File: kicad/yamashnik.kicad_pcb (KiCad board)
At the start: 2 copper layers, 43 x 25.8 mm, 13 parts, among them J1 USB_AM_PCB, P1 CONN_5, P2 CONN_4, U1 6N137, U2 6N138, U3 CP2102

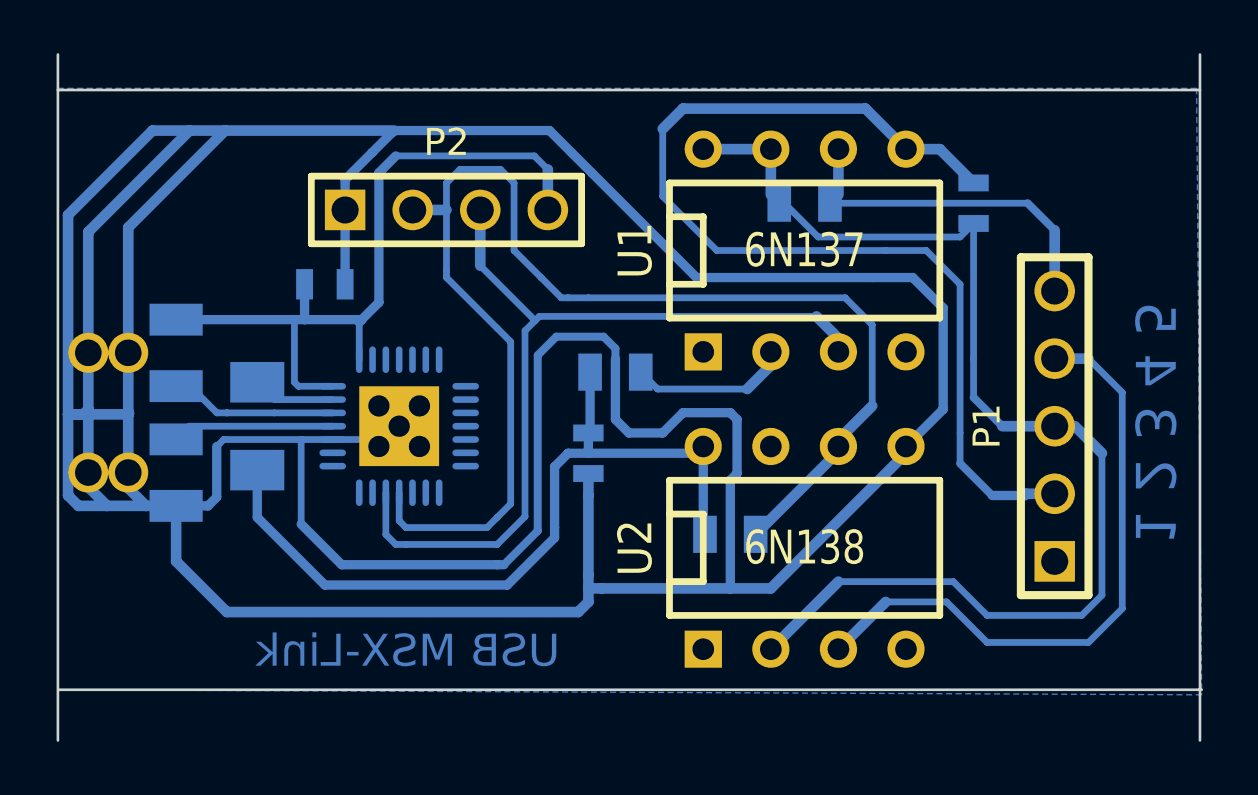
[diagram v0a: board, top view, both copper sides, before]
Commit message: recovered kicad_pcb, updated edge cuts
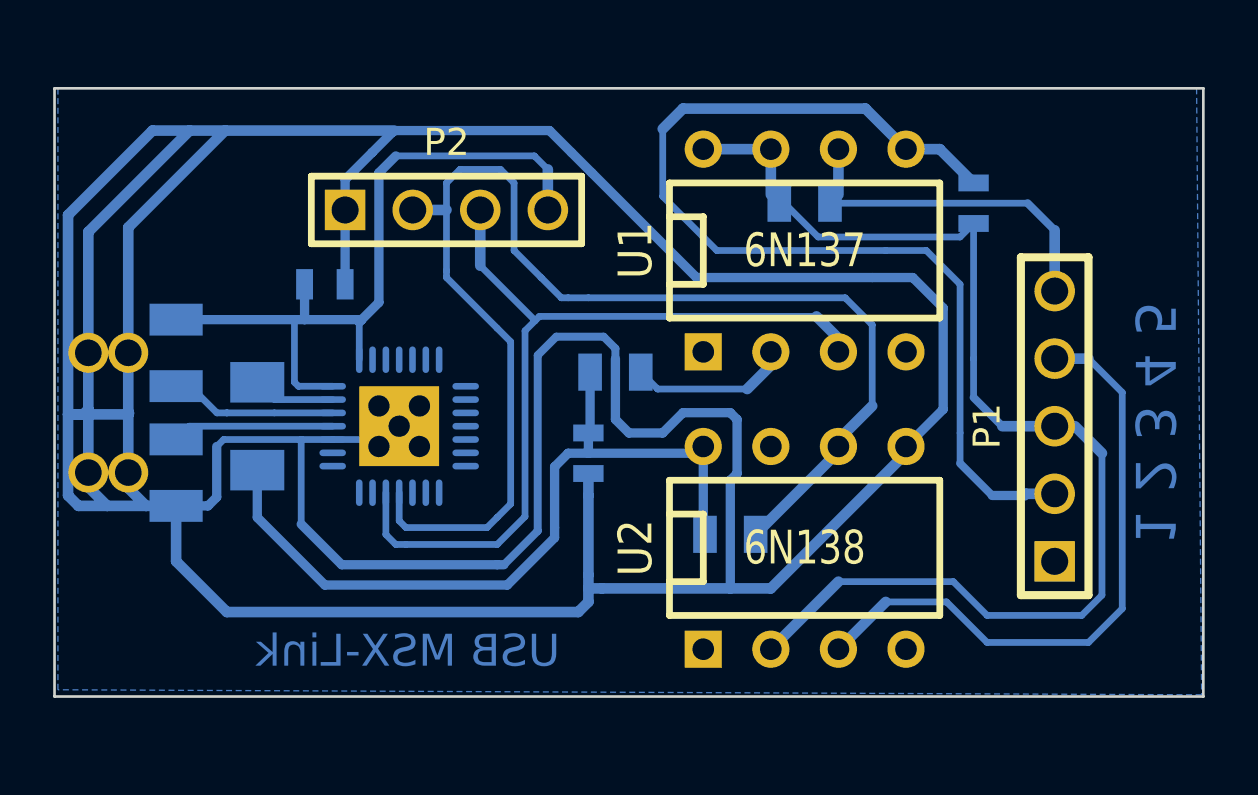
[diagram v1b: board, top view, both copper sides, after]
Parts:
- R3: value 750 -> 11K
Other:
- board size 43 x 25.8 mm -> 43.2 x 22.9 mm
